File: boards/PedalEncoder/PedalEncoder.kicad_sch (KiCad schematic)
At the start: 33 parts, among them J1 Pwr, J2 Control, J3 Switch, J4 ISP, J5 Pedal, J6 MIDI Out, J7 I2C, Q1 BC547, U1 4069, U2 ATmega48-20P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

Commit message: New PCB version of PedalEncoder
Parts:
- D1, D2: footprint Diode_THT:D_DO-41_SOD81_P2.54mm_Vertical_AnodeUp -> Diode_THT:D_DO-41_SOD81_P3.81mm_Vertical_AnodeUp
- D3: footprint Diode_THT:D_DO-15_P2.54mm_Vertical_AnodeUp -> Diode_THT:D_DO-15_P3.81mm_Vertical_AnodeUp
- J1: footprint Connector_PinSocket_2.54mm:PinSocket_1x02_P2.54mm_Vertical -> Connector_PinHeader_2.54mm:PinHeader_1x02_P2.54mm_Vertical
- Q1: footprint Package_TO_SOT_THT:TO-92_Inline -> Package_TO_SOT_THT:TO-92_Inline_Wide
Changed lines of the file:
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@@
 			)
 		)
-		(property "Footprint" "Diode_THT:D_DO-41_SOD81_P2.54mm_Vertical_AnodeUp"
+		(property "Footprint" "Diode_THT:D_DO-41_SOD81_P3.81mm_Vertical_AnodeUp"
 			(at 67.31 34.925 0)
 			(effects
@@
 			)
 		)
-		(property "Footprint" "Diode_THT:D_DO-41_SOD81_P2.54mm_Vertical_AnodeUp"
+		(property "Footprint" "Diode_THT:D_DO-41_SOD81_P3.81mm_Vertical_AnodeUp"
 			(at 67.31 24.765 0)
 			(effects
@@
 			)
 		)
-		(property "Footprint" "Diode_THT:D_DO-15_P2.54mm_Vertical_AnodeUp"
+		(property "Footprint" "Diode_THT:D_DO-15_P3.81mm_Vertical_AnodeUp"
 			(at 60.96 64.77 0)
 			(effects
@@
 			)
 		)
-		(property "Footprint" "Package_TO_SOT_THT:TO-92_Inline"
+		(property "Footprint" "Package_TO_SOT_THT:TO-92_Inline_Wide"
 			(at 257.81 60.325 0)
 			(effects
@@
 			)
 		)
-		(property "Footprint" "Connector_PinSocket_2.54mm:PinSocket_1x02_P2.54mm_Vertical"
+		(property "Footprint" "Connector_PinHeader_2.54mm:PinHeader_1x02_P2.54mm_Vertical"
 			(at 21.59 38.1 0)
 			(effects

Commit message: Using custom TO220 cooler, fixed and finished several PCBs
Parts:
- HS1: footprint Heatsink:Heatsink_AAVID_576802B03900G -> Custom_Heatsinks:Heatsink_Aavid_TO-220_H12.7mm
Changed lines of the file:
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@@
 			)
 		)
-		(property "Footprint" "Heatsink:Heatsink_AAVID_576802B03900G"
+		(property "Footprint" "Custom_Heatsinks:Heatsink_Aavid_TO-220_H12.7mm"
 			(at 101.9048 20.32 0)
 			(effects

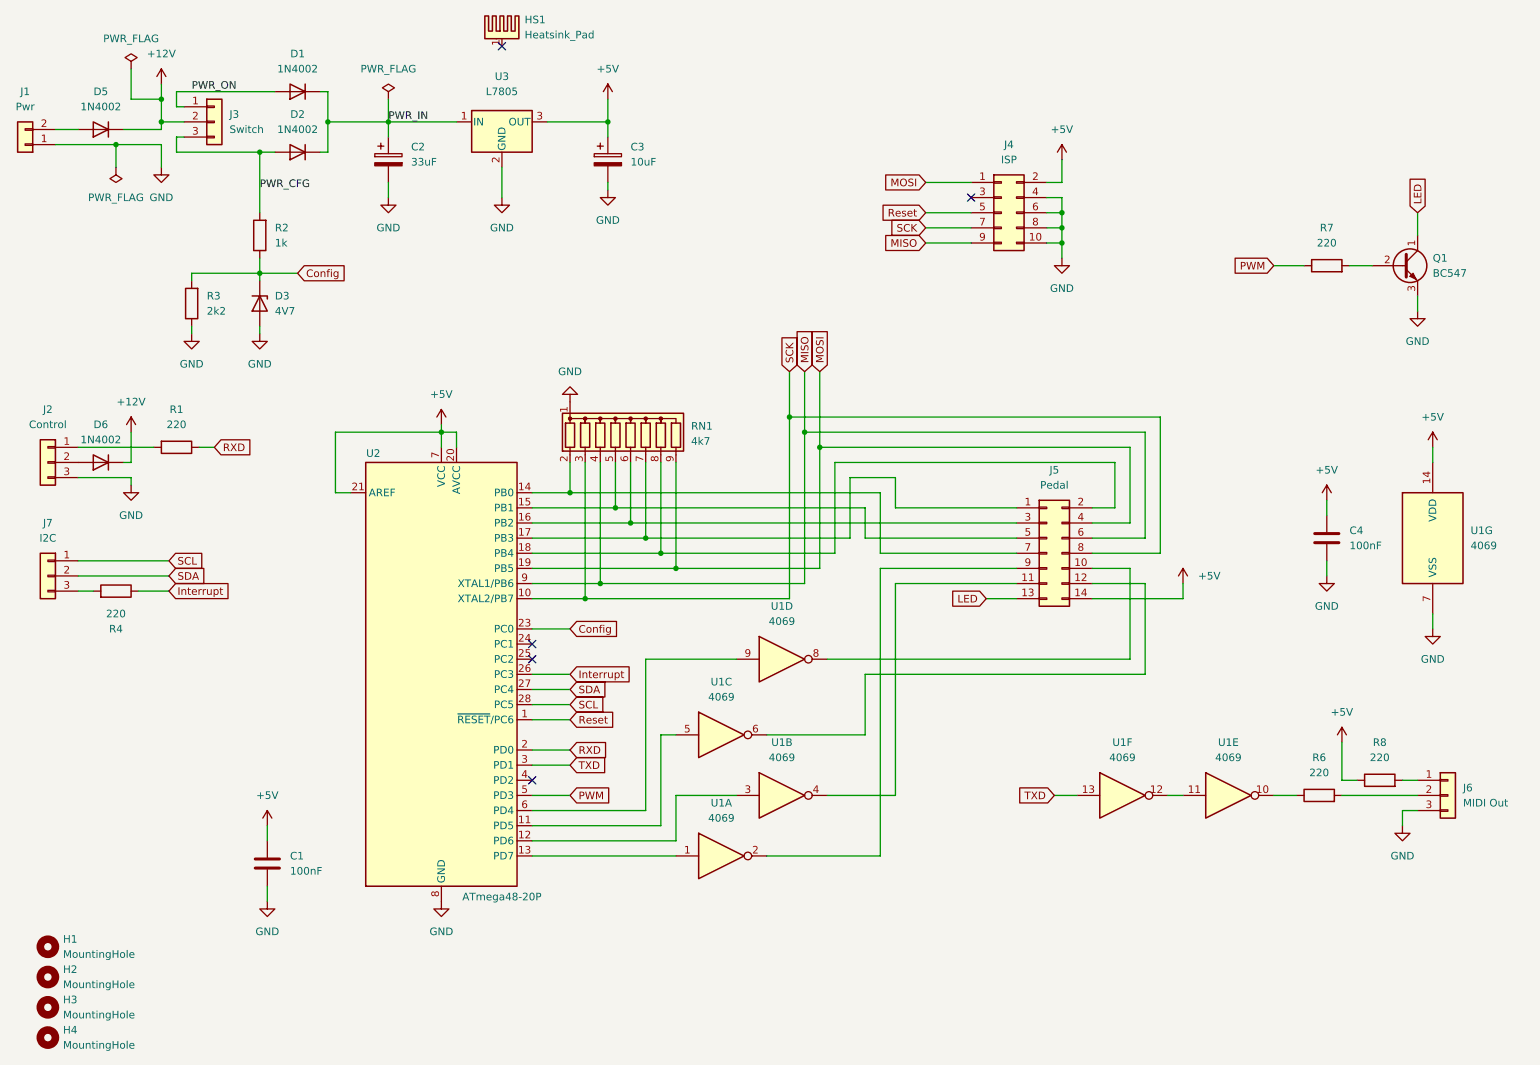
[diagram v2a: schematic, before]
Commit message: Fixed interrupt line to use open collector, added pullups to I2C lines
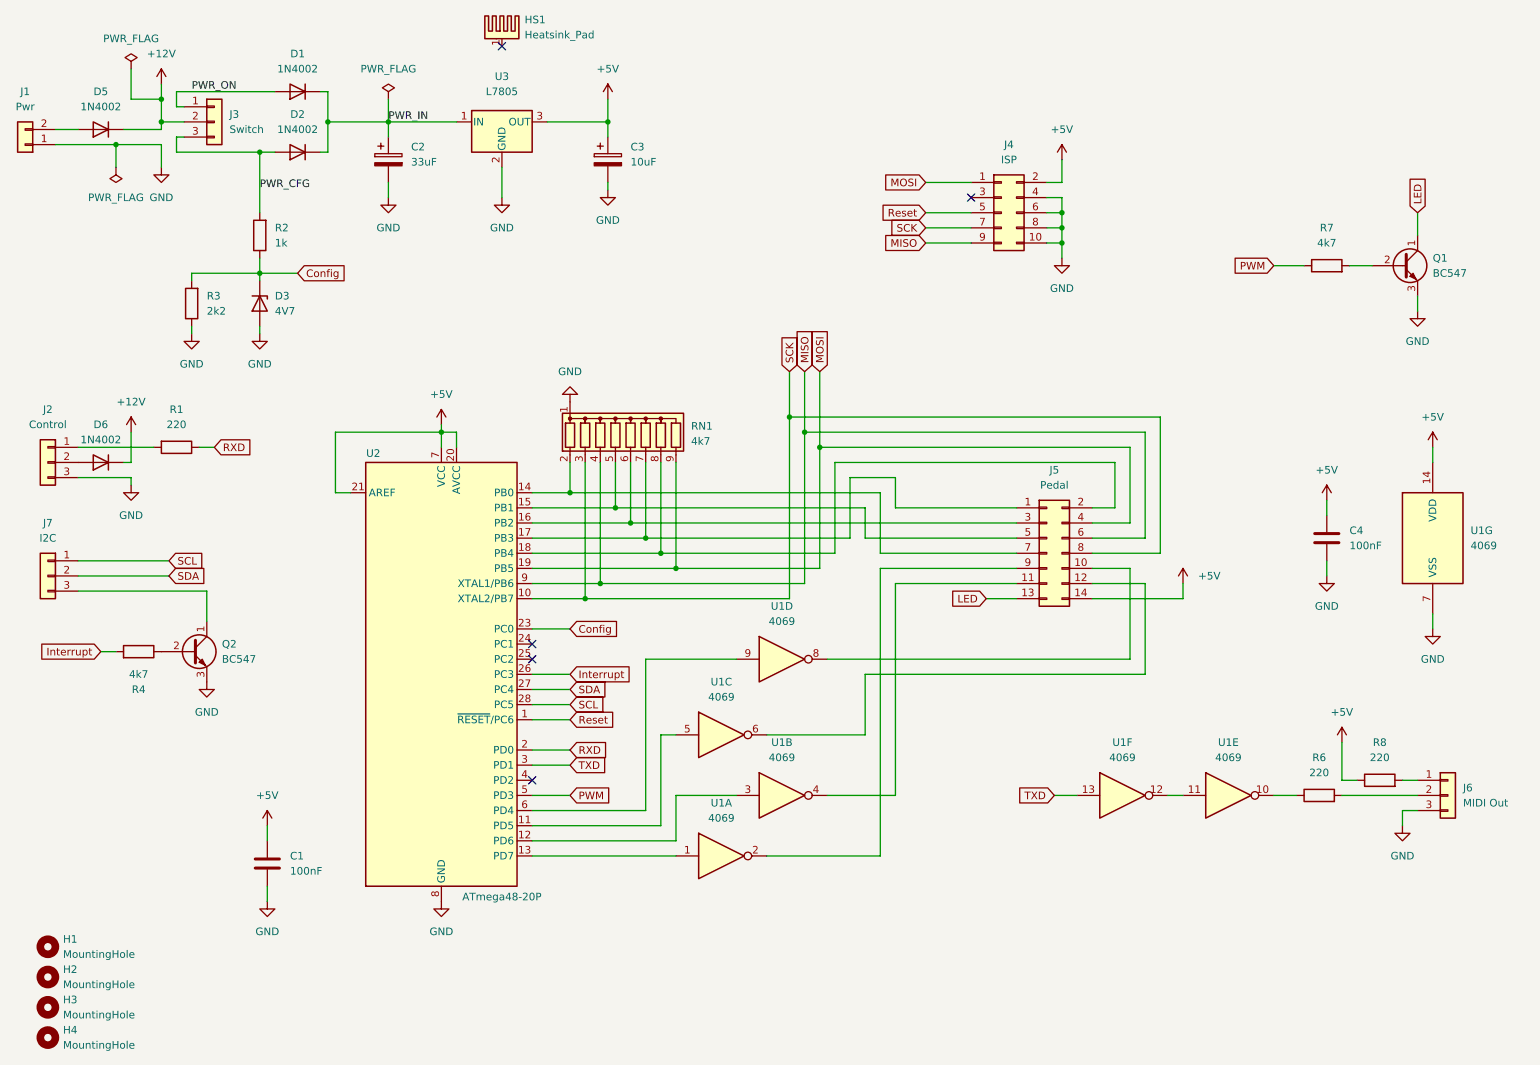
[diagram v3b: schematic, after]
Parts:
- added Q2: BC547, Package_TO_SOT_THT:TO-92_Inline_Wide, symbol Transistor_BJT:BC547
- R4, R7: value 220 -> 4k7
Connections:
- net GND: now also Q2.3 (E)
- net Interrupt: now also R4.2; no longer R4.1
- net at J7.3 (Pin_3): now also Q2.1 (C); no longer R4.2
- new net: Q2.2 (B), R4.1
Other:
- moved on the sheet: R4
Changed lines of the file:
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@@
 	(wire
 		(pts
+			(xy 34.29 123.19) (xy 36.83 123.19)
+		)
+		(stroke
+			(width 0)
+			(type default)
+		)
+	)
+	(wire
+		(pts
 			(xy 118.11 111.76) (xy 118.11 91.44)
 		)
@@
 	(wire
 		(pts
+			(xy 52.07 113.03) (xy 52.07 118.11)
+		)
+		(stroke
+			(width 0)
+			(type default)
+		)
+	)
+	(wire
+		(pts
 			(xy 38.1 35.56) (xy 44.45 35.56)
 		)
@@
 	(wire
 		(pts
-			(xy 30.48 113.03) (xy 33.02 113.03)
+			(xy 30.48 113.03) (xy 52.07 113.03)
 		)
 		(stroke
@@
 	(wire
 		(pts
-			(xy 40.64 113.03) (xy 45.72 113.03)
-		)
-		(stroke
-			(width 0)
-			(type default)
-		)
-	)
-	(wire
-		(pts
 			(xy 157.48 91.44) (xy 157.48 106.68)
 		)
@@
 	(global_label "Interrupt"
 		(shape input)
-		(at 45.72 113.03 0)
+		(at 34.29 123.19 180)
 		(fields_autoplaced yes)
 		(effects
@@
 				(size 1.27 1.27)
 			)
-			(justify left)
+			(justify right)
 		)
 		(property "Intersheetrefs" "${INTERSHEET_REFS}"
-			(at 56.8694 113.03 0)
+			(at 23.1406 123.19 0)
 			(effects
 				(font
 					(size 1.27 1.27)
 				)
-				(justify left)
+				(justify right)
 				(hide yes)
 			)
@@
 	)
 	(symbol
+		(lib_id "Transistor_BJT:BC547")
+		(at 49.53 123.19 0)
+		(unit 1)
+		(exclude_from_sim no)
+		(in_bom yes)
+		(on_board yes)
+		(dnp no)
+		(fields_autoplaced yes)
+		(property "Reference" "Q2"
+			(at 54.61 121.9199 0)
+			(effects
+				(font
+					(size 1.27 1.27)
+				)
+				(justify left)
+			)
+		)
+		(property "Value" "BC547"
+			(at 54.61 124.4599 0)
+			(effects
+				(font
+					(size 1.27 1.27)
+				)
+				(justify left)
+			)
+		)
+		(property "Footprint" "Package_TO_SOT_THT:TO-92_Inline_Wide"
+			(at 54.61 125.095 0)
+			(effects
+				(font
+					(size 1.27 1.27)
+					(italic yes)
+				)
+				(justify left)
+				(hide yes)
+			)
+		)
+		(property "Datasheet" "https://www.onsemi.com/pub/Collateral/BC550-D.pdf"
+			(at 49.53 123.19 0)
+			(effects
+				(font
+					(size 1.27 1.27)
+				)
+				(justify left)
+				(hide yes)
+			)
+		)
+		(property "Description" "0.1A Ic, 45V Vce, Small Signal NPN Transistor, TO-92"
+			(at 49.53 123.19 0)
+			(effects
+				(font
+					(size 1.27 1.27)
+				)
+				(hide yes)
+			)
+		)
+		(pin "1"
+		)
+		(pin "2"
+		)
+		(pin "3"
+		)
+		(instances
+			(project "PedalEncoder"
+				(path "/31308be9-b013-4abe-98e2-32d430dea950"
+					(reference "Q2")
+					(unit 1)
+				)
+			)
+		)
+	)
+	(symbol
 		(lib_id "Regulator_Linear:L7805")
 		(at 101.6 34.29 0)
@@
 			)
 		)
-		(property "Value" "220"
+		(property "Value" "4k7"
 			(at 240.03 54.61 90)
 			(effects
@@
 	)
 	(symbol
+		(lib_id "power:GND")
+		(at 52.07 128.27 0)
+		(unit 1)
+		(exclude_from_sim no)
+		(in_bom yes)
+		(on_board yes)
+		(dnp no)
+		(fields_autoplaced yes)
+		(property "Reference" "#PWR018"
+			(at 52.07 134.62 0)
+			(effects
+				(font
+					(size 1.27 1.27)
+				)
+				(hide yes)
+			)
+		)
+		(property "Value" "GND"
+			(at 52.07 133.35 0)
+			(effects
+				(font
+					(size 1.27 1.27)
+				)
+			)
+		)
+		(property "Footprint" ""
+			(at 52.07 128.27 0)
+			(effects
+				(font
+					(size 1.27 1.27)
+				)
+				(hide yes)
+			)
+		)
+		(property "Datasheet" ""
+			(at 52.07 128.27 0)
+			(effects
+				(font
+					(size 1.27 1.27)
+				)
+				(hide yes)
+			)
+		)
+		(property "Description" "Power symbol creates a global label with name \"GND\" , ground"
+			(at 52.07 128.27 0)
+			(effects
+				(font
+					(size 1.27 1.27)
+				)
+				(hide yes)
+			)
+		)
+		(pin "1"
+		)
+		(instances
+			(project "PedalEncoder"
+				(path "/31308be9-b013-4abe-98e2-32d430dea950"
+					(reference "#PWR018")
+					(unit 1)
+				)
+			)
+		)
+	)
+	(symbol
 		(lib_id "Connector_Generic:Conn_02x07_Odd_Even")
 		(at 193.04 106.68 0)
@@
 	(symbol
 		(lib_id "Device:R")
-		(at 36.83 113.03 270)
+		(at 40.64 123.19 270)
 		(mirror x)
 		(unit 1)
@@
 		(dnp no)
 		(property "Reference" "R4"
-			(at 36.83 119.38 90)
+			(at 40.64 129.54 90)
 			(effects
 				(font
@@
 			)
 		)
-		(property "Value" "220"
-			(at 36.83 116.84 90)
+		(property "Value" "4k7"
+			(at 40.64 127 90)
 			(effects
 				(font
@@
 		)
 		(property "Footprint" "Resistor_THT:R_Axial_DIN0204_L3.6mm_D1.6mm_P2.54mm_Vertical"
-			(at 36.83 114.808 90)
+			(at 40.64 124.968 90)
 			(effects
 				(font
@@
 		)
 		(property "Datasheet" "~"
-			(at 36.83 113.03 0)
+			(at 40.64 123.19 0)
 			(effects
 				(font
@@
 		)
 		(property "Description" "Resistor"
-			(at 36.83 113.03 0)
+			(at 40.64 123.19 0)
 			(effects
 				(font

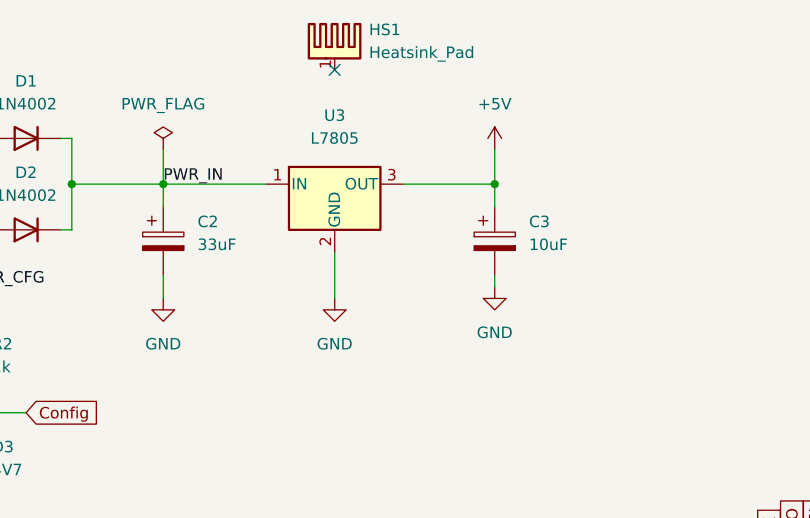
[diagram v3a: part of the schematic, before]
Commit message: Added bypass caps to power supplies, use cheaper MAX232 IC.
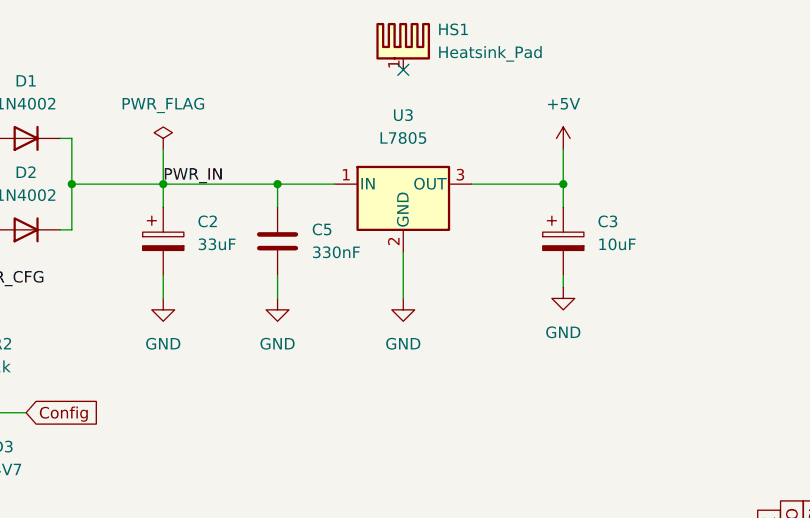
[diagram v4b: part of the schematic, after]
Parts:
- added C5: 330nF, Capacitor_THT:C_Disc_D7.5mm_W2.5mm_P5.00mm, symbol Device:C
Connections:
- net GND: now also C5.2
- net PWR_IN: now also C5.1
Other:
- moved on the sheet: C3, HS1, U3

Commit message: Updated design rules to 0.32mm template and exported Gerber files
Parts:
- R1, R7: footprint Resistor_THT:R_Axial_DIN0204_L3.6mm_D1.6mm_P7.62mm_Horizontal -> Resistor_THT:R_Axial_DIN0207_L6.3mm_D2.5mm_P10.16mm_Horizontal
- R2: footprint Resistor_THT:R_Axial_DIN0204_L3.6mm_D1.6mm_P7.62mm_Horizontal -> Resistor_THT:R_Axial_DIN0207_L6.3mm_D2.5mm_P2.54mm_Vertical
- R3, R4, R6, R8: footprint Resistor_THT:R_Axial_DIN0204_L3.6mm_D1.6mm_P2.54mm_Vertical -> Resistor_THT:R_Axial_DIN0207_L6.3mm_D2.5mm_P2.54mm_Vertical
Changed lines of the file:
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@@
 			)
 		)
-		(property "Footprint" "Resistor_THT:R_Axial_DIN0204_L3.6mm_D1.6mm_P2.54mm_Vertical"
+		(property "Footprint" "Resistor_THT:R_Axial_DIN0207_L6.3mm_D2.5mm_P2.54mm_Vertical"
 			(at 238.76 149.098 90)
 			(effects
@@
 			)
 		)
-		(property "Footprint" "Resistor_THT:R_Axial_DIN0204_L3.6mm_D1.6mm_P7.62mm_Horizontal"
+		(property "Footprint" "Resistor_THT:R_Axial_DIN0207_L6.3mm_D2.5mm_P10.16mm_Horizontal"
 			(at 46.99 87.122 90)
 			(effects
@@
 			)
 		)
-		(property "Footprint" "Resistor_THT:R_Axial_DIN0204_L3.6mm_D1.6mm_P7.62mm_Horizontal"
+		(property "Footprint" "Resistor_THT:R_Axial_DIN0207_L6.3mm_D2.5mm_P2.54mm_Vertical"
 			(at 62.738 53.34 90)
 			(effects
@@
 			)
 		)
-		(property "Footprint" "Resistor_THT:R_Axial_DIN0204_L3.6mm_D1.6mm_P2.54mm_Vertical"
+		(property "Footprint" "Resistor_THT:R_Axial_DIN0207_L6.3mm_D2.5mm_P2.54mm_Vertical"
 			(at 248.92 146.558 90)
 			(effects
@@
 			)
 		)
-		(property "Footprint" "Resistor_THT:R_Axial_DIN0204_L3.6mm_D1.6mm_P2.54mm_Vertical"
+		(property "Footprint" "Resistor_THT:R_Axial_DIN0207_L6.3mm_D2.5mm_P2.54mm_Vertical"
 			(at 51.308 64.77 90)
 			(effects
@@
 			)
 		)
-		(property "Footprint" "Resistor_THT:R_Axial_DIN0204_L3.6mm_D1.6mm_P7.62mm_Horizontal"
+		(property "Footprint" "Resistor_THT:R_Axial_DIN0207_L6.3mm_D2.5mm_P10.16mm_Horizontal"
 			(at 240.03 60.198 90)
 			(effects
@@
 			)
 		)
-		(property "Footprint" "Resistor_THT:R_Axial_DIN0204_L3.6mm_D1.6mm_P2.54mm_Vertical"
+		(property "Footprint" "Resistor_THT:R_Axial_DIN0207_L6.3mm_D2.5mm_P2.54mm_Vertical"
 			(at 40.64 124.968 90)
 			(effects

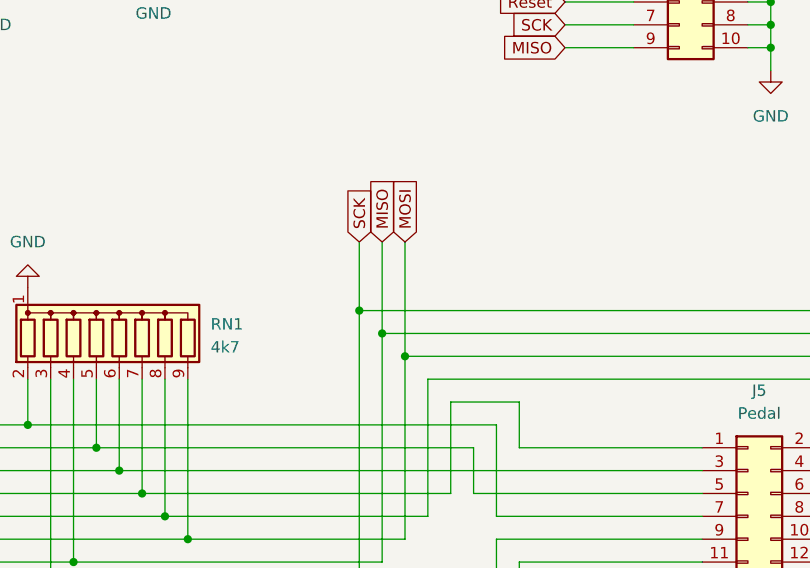
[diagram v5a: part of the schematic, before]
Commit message: Fixed PedalEncoder ISP hedaer schematics, added Errata notes
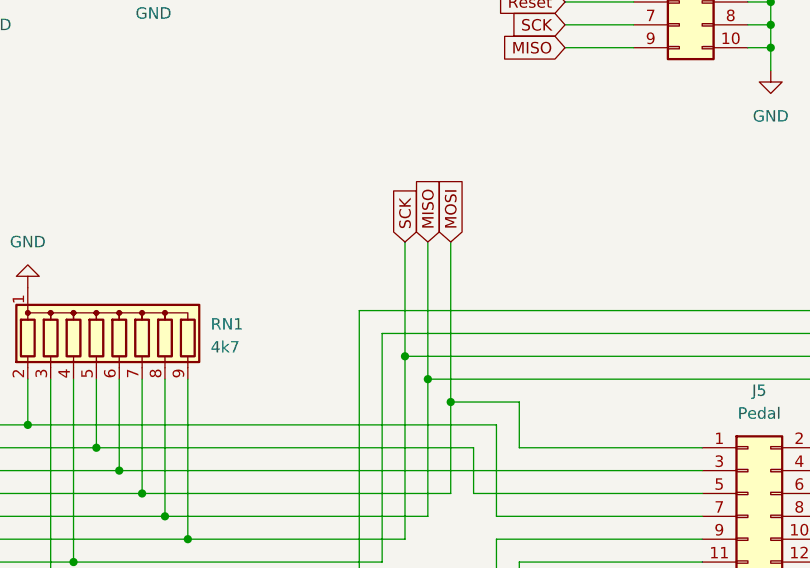
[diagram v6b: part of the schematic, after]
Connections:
- net MISO: now also J5.2 (Pin_2), RN1.8 (R7), U2.18 (PB4); no longer J5.6 (Pin_6), RN1.4 (R3), U2.9 (XTAL1/PB6)
- net MOSI: now also J5.1 (Pin_1), RN1.7 (R6), U2.17 (PB3); no longer J5.4 (Pin_4), RN1.9 (R8), U2.19 (PB5)
- net SCK: now also J5.4 (Pin_4), RN1.9 (R8), U2.19 (PB5); no longer J5.8 (Pin_8), RN1.3 (R2), U2.10 (XTAL2/PB7)
- new net: J5.8 (Pin_8), RN1.3 (R2), U2.10 (XTAL2/PB7)
- new net: J5.6 (Pin_6), RN1.4 (R3), U2.9 (XTAL1/PB6)
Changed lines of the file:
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@@
+	)
+	(junction
+		(at 157.48 91.44)
+		(diameter 0)
+		(color 0 0 0 0)
 	)
 	(junction
@@
 	)
 	(junction
+		(at 160.02 93.98)
+		(diameter 0)
+		(color 0 0 0 0)
+	)
+	(junction
 		(at 44.45 34.29)
 		(diameter 0)
@@
 	)
 	(junction
-		(at 149.86 83.82)
-		(diameter 0)
-		(color 0 0 0 0)
-	)
-	(junction
 		(at 154.94 88.9)
 		(diameter 0)
 		(color 0 0 0 0)
 	)
-	(junction
-		(at 152.4 86.36)
-		(diameter 0)
-		(color 0 0 0 0)
-	)
 	(no_connect
 		(at 180.34 46.99)
@@
 	(wire
 		(pts
-			(xy 149.86 76.2) (xy 149.86 83.82)
-		)
-		(stroke
-			(width 0)
-			(type default)
-		)
-	)
-	(wire
-		(pts
 			(xy 30.48 110.49) (xy 45.72 110.49)
 		)
@@
 	(wire
 		(pts
+			(xy 160.02 76.2) (xy 160.02 93.98)
+		)
+		(stroke
+			(width 0)
+			(type default)
+		)
+	)
+	(wire
+		(pts
 			(xy 60.96 39.37) (xy 60.96 49.53)
 		)
@@
 	(wire
 		(pts
-			(xy 152.4 76.2) (xy 152.4 86.36)
-		)
-		(stroke
-			(width 0)
-			(type default)
-		)
-	)
-	(wire
-		(pts
 			(xy 60.96 68.58) (xy 60.96 69.85)
 		)
@@
 		(pts
 			(xy 44.45 38.1) (xy 44.45 41.91)
+		)
+		(stroke
+			(width 0)
+			(type default)
+		)
+	)
+	(wire
+		(pts
+			(xy 157.48 76.2) (xy 157.48 91.44)
 		)
 		(stroke
@@
 	(global_label "MOSI"
 		(shape input)
-		(at 154.94 76.2 90)
+		(at 160.02 76.2 90)
 		(fields_autoplaced yes)
 		(effects
@@
 		)
 		(property "Intersheetrefs" "${INTERSHEET_REFS}"
-			(at 155.0194 69.1907 90)
+			(at 160.0994 69.1907 90)
 			(effects
 				(font
@@
 	(global_label "MISO"
 		(shape input)
-		(at 152.4 76.2 90)
+		(at 157.48 76.2 90)
 		(fields_autoplaced yes)
 		(effects
@@
 		)
 		(property "Intersheetrefs" "${INTERSHEET_REFS}"
-			(at 152.4794 69.1907 90)
+			(at 157.5594 69.1907 90)
 			(effects
 				(font
@@
 	(global_label "SCK"
 		(shape input)
-		(at 149.86 76.2 90)
+		(at 154.94 76.2 90)
 		(fields_autoplaced yes)
 		(effects
@@
 		)
 		(property "Intersheetrefs" "${INTERSHEET_REFS}"
-			(at 149.9394 70.0374 90)
+			(at 155.0194 70.0374 90)
 			(effects
 				(font
